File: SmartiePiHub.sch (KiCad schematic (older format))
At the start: 26 parts, among them P1 Conn_02x20_Odd_Even

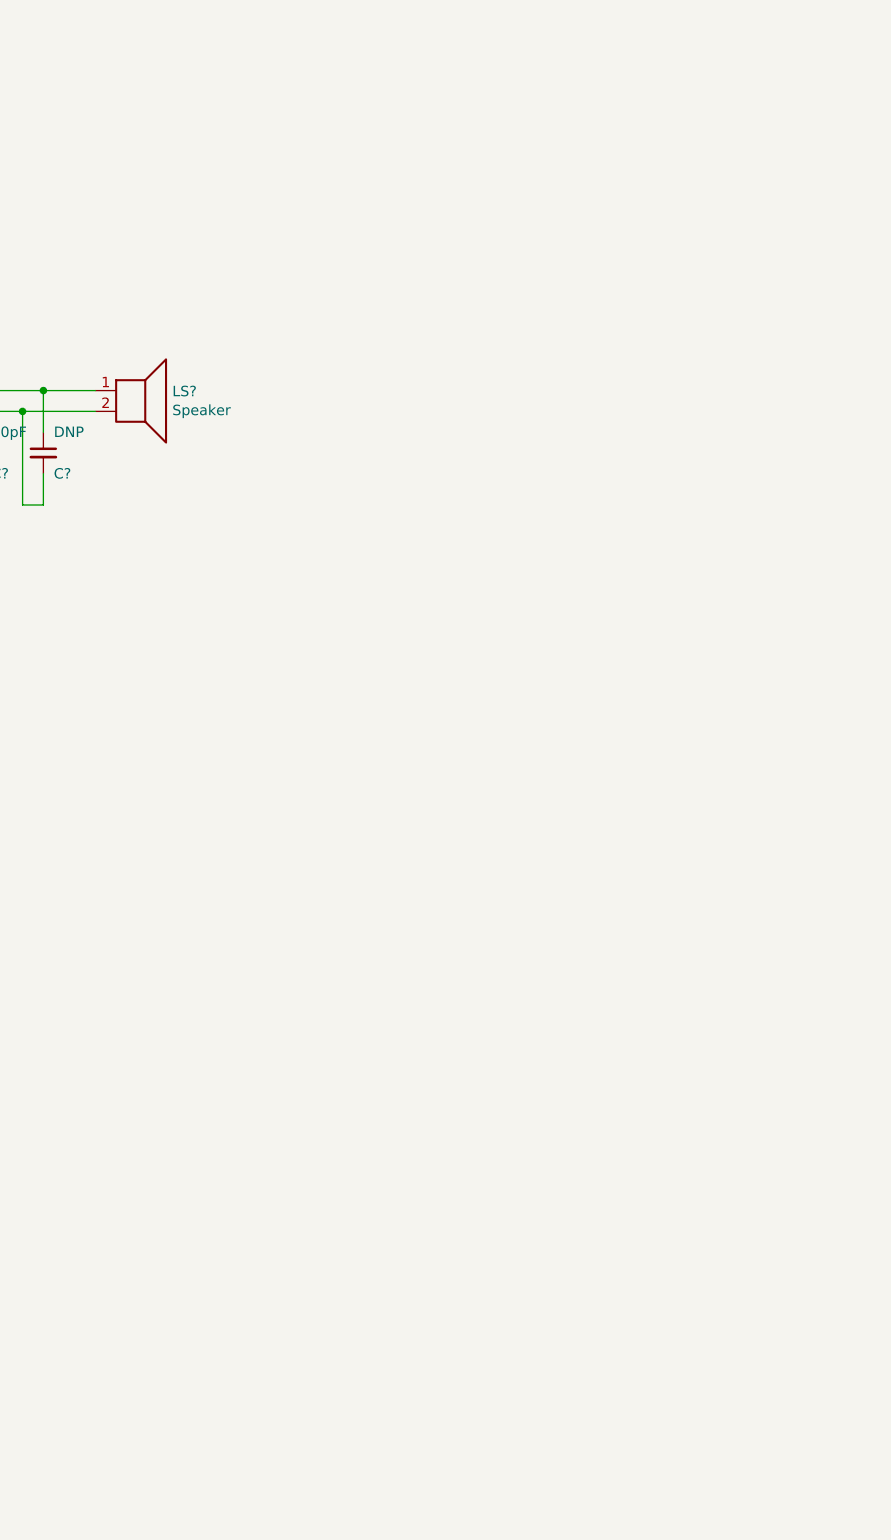
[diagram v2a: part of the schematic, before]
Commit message: added ina219 and mcp73833
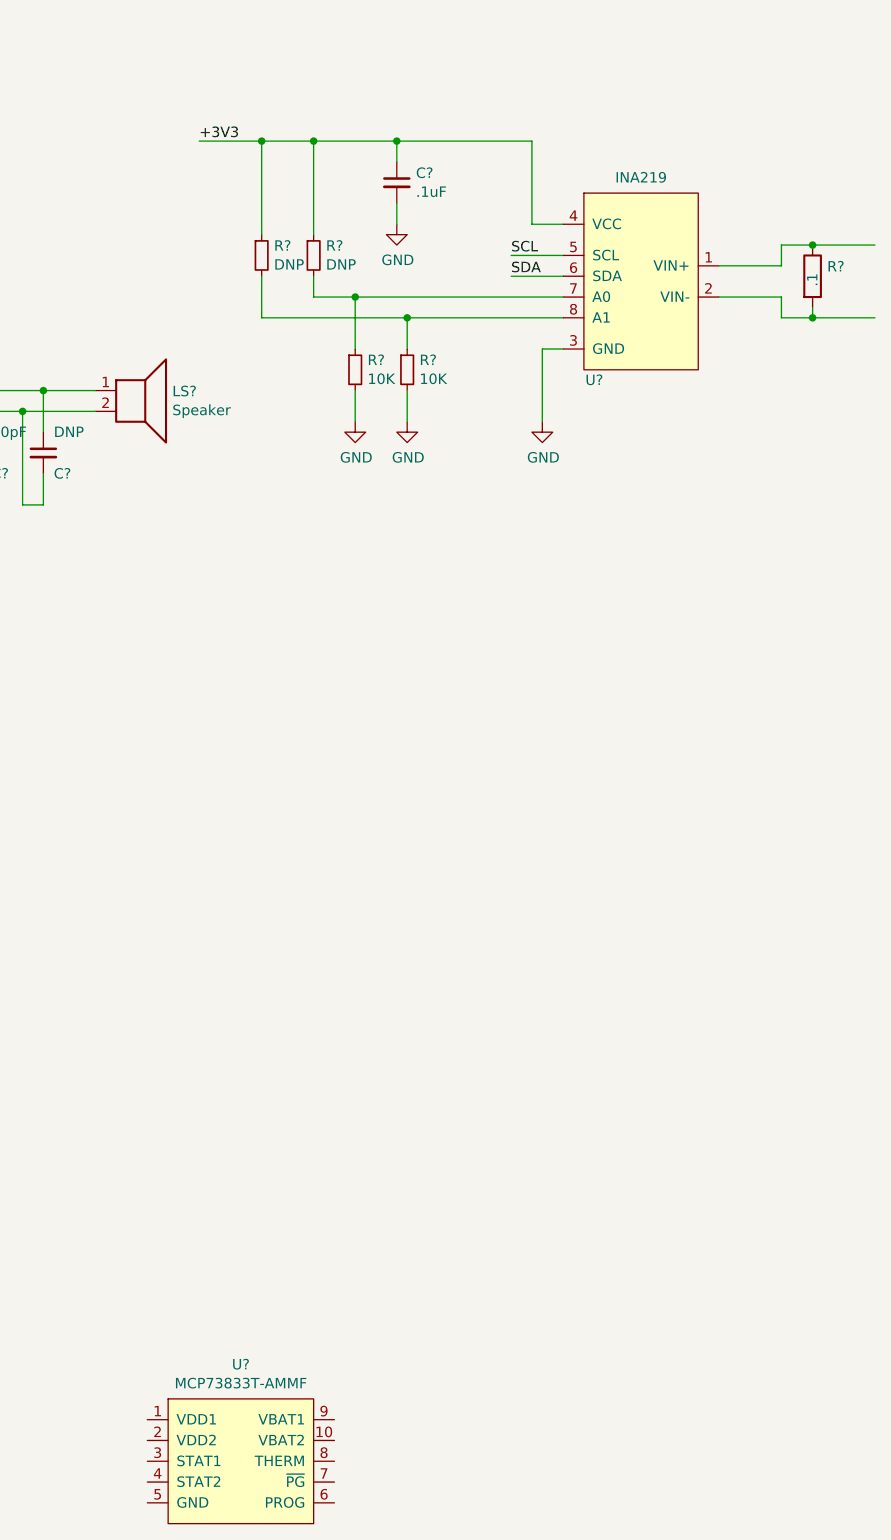
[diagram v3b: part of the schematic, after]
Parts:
- added C?: .1uF, symbol Device:C_Small
- added R? (x2): DNP, symbol Device:R_Small
- added R? (x2): 10K, symbol Device:R_Small
- added R?: .1, symbol Device:R
- added U?: INA219, symbol smartie-pi-hub:INA219
- added U?: MCP73833T-AMMF, symbol smartie-pi-hub:MCP73833T-AMMF
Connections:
- net +3V3: now also C?.1, R?.1, R?.1, U?.4 (VCC)
- net GND: now also C?.2, R?.2, R?.2, U?.3 (GND)
- new net: R?.1, U?.1 (VIN+)
- new net: R?.2, U?.2 (VIN-)
- new net: R?.1, R?.2, U?.7 (A0)
- new net: R?.1, R?.2, U?.8 (A1)
- new net SCL: U?.5 (SCL)
- new net SDA: U?.6 (SDA)
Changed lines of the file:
@@
 EELAYER 30 0
 EELAYER END
-$Descr A4 11693 8268
+$Descr A3 16535 11693
 encoding utf-8
 Sheet 1 1
@@
 	1    0    0    -1
 $EndComp
+$Comp
+L smartie-pi-hub:INA219 U?
+U 1 1 5EDB41F3
+P 13750 2050
+F 0 "U?" H 13500 1700 50  0000 C CNN
+F 1 "INA219" H 13725 2674 50  0000 C CNN
+F 2 "" H 13750 2050 50  0001 C CNN
+F 3 "" H 13750 2050 50  0001 C CNN
+	1    13750 2050
+	1    0    0    -1
+$EndComp
+$Comp
+L Device:C_Small C?
+U 1 1 5EDB4D7C
+P 12550 1450
+F 0 "C?" H 12642 1496 50  0000 L CNN
+F 1 ".1uF" H 12642 1405 50  0000 L CNN
+F 2 "" H 12550 1450 50  0001 C CNN
+F 3 "~" H 12550 1450 50  0001 C CNN
+	1    12550 1450
+	1    0    0    -1
+$EndComp
+$Comp
+L Device:R_Small R?
+U 1 1 5EDB5D3C
+P 12150 1800
+F 0 "R?" H 12209 1846 50  0000 L CNN
+F 1 "DNP" H 12209 1755 50  0000 L CNN
+F 2 "" H 12150 1800 50  0001 C CNN
+F 3 "~" H 12150 1800 50  0001 C CNN
+	1    12150 1800
+	1    0    0    -1
+$EndComp
+$Comp
+L Device:R_Small R?
+U 1 1 5EDB6AA8
+P 11900 1800
+F 0 "R?" H 11959 1846 50  0000 L CNN
+F 1 "DNP" H 11959 1755 50  0000 L CNN
+F 2 "" H 11900 1800 50  0001 C CNN
+F 3 "~" H 11900 1800 50  0001 C CNN
+	1    11900 1800
+	1    0    0    -1
+$EndComp
+$Comp
+L Device:R_Small R?
+U 1 1 5EDB758D
+P 12350 2350
+F 0 "R?" H 12409 2396 50  0000 L CNN
+F 1 "10K" H 12409 2305 50  0000 L CNN
+F 2 "" H 12350 2350 50  0001 C CNN
+F 3 "~" H 12350 2350 50  0001 C CNN
+	1    12350 2350
+	1    0    0    -1
+$EndComp
+$Comp
+L Device:R_Small R?
+U 1 1 5EDB7587
+P 12600 2350
+F 0 "R?" H 12659 2396 50  0000 L CNN
+F 1 "10K" H 12659 2305 50  0000 L CNN
+F 2 "" H 12600 2350 50  0001 C CNN
+F 3 "~" H 12600 2350 50  0001 C CNN
+	1    12600 2350
+	1    0    0    -1
+$EndComp
+Wire Wire Line
+	13350 2250 13250 2250
+$Comp
+L power:GND #PWR?
+U 1 1 5EDC7C5A
+P 13250 2600
+F 0 "#PWR?" H 13250 2350 50  0001 C CNN
+F 1 "GND" H 13255 2427 50  0000 C CNN
+F 2 "" H 13250 2600 50  0001 C CNN
+F 3 "" H 13250 2600 50  0001 C CNN
+	1    13250 2600
+	1    0    0    -1
+$EndComp
+Wire Wire Line
+	13250 2250 13250 2600
+$Comp
+L power:GND #PWR?
+U 1 1 5EDD0454
+P 12600 2600
+F 0 "#PWR?" H 12600 2350 50  0001 C CNN
+F 1 "GND" H 12605 2427 50  0000 C CNN
+F 2 "" H 12600 2600 50  0001 C CNN
+F 3 "" H 12600 2600 50  0001 C CNN
+	1    12600 2600
+	1    0    0    -1
+$EndComp
+$Comp
+L power:GND #PWR?
+U 1 1 5EDD09EB
+P 12350 2600
+F 0 "#PWR?" H 12350 2350 50  0001 C CNN
+F 1 "GND" H 12355 2427 50  0000 C CNN
+F 2 "" H 12350 2600 50  0001 C CNN
+F 3 "" H 12350 2600 50  0001 C CNN
+	1    12350 2600
+	1    0    0    -1
+$EndComp
+Wire Wire Line
+	12350 2600 12350 2450
+Wire Wire Line
+	12600 2450 12600 2600
+Wire Wire Line
+	13350 2100 12600 2100
+Wire Wire Line
+	11900 2100 11900 1900
+Wire Wire Line
+	12150 1900 12150 2000
+Wire Wire Line
+	12150 2000 12350 2000
+Wire Wire Line
+	12600 2250 12600 2100
+Connection ~ 12600 2100
+Wire Wire Line
+	12600 2100 11900 2100
+Wire Wire Line
+	12350 2000 12350 2250
+Connection ~ 12350 2000
+Wire Wire Line
+	12350 2000 13350 2000
+Wire Wire Line
+	12550 1550 12550 1650
+$Comp
+L power:GND #PWR?
+U 1 1 5EE0BE4E
+P 12550 1650
+F 0 "#PWR?" H 12550 1400 50  0001 C CNN
+F 1 "GND" H 12555 1477 50  0000 C CNN
+F 2 "" H 12550 1650 50  0001 C CNN
+F 3 "" H 12550 1650 50  0001 C CNN
+	1    12550 1650
+	1    0    0    -1
+$EndComp
+Wire Wire Line
+	12150 1700 12150 1250
+Wire Wire Line
+	12150 1250 11900 1250
+Wire Wire Line
+	11900 1250 11900 1700
+Connection ~ 11900 1250
+Wire Wire Line
+	11900 1250 11600 1250
+Wire Wire Line
+	12550 1350 12550 1250
+Wire Wire Line
+	12550 1250 12150 1250
+Connection ~ 12150 1250
+Wire Wire Line
+	13350 1650 13200 1650
+Wire Wire Line
+	13200 1650 13200 1250
+Wire Wire Line
+	13200 1250 12550 1250
+Connection ~ 12550 1250
+Text Label 11600 1250 0    50   ~ 0
++3V3
+Wire Wire Line
+	13350 1800 13100 1800
+Wire Wire Line
+	13350 1900 13100 1900
+Text Label 13100 1800 0    50   ~ 0
+SCL
+Text Label 13100 1900 0    50   ~ 0
+SDA
+$Comp
+L Device:R R?
+U 1 1 5EE4572A
+P 14550 1900
+F 0 "R?" H 14620 1946 50  0000 L CNN
+F 1 ".1" V 14550 1850 50  0000 L CNN
+F 2 "" V 14480 1900 50  0001 C CNN
+F 3 "~" H 14550 1900 50  0001 C CNN
+	1    14550 1900
+	1    0    0    -1
+$EndComp
+Wire Wire Line
+	14550 1750 14400 1750
+Wire Wire Line
+	14400 1750 14400 1850
+Wire Wire Line
+	14400 1850 14100 1850
+Wire Wire Line
+	14100 2000 14400 2000
+Wire Wire Line
+	14400 2000 14400 2100
+Wire Wire Line
+	14400 2100 14550 2100
+Wire Wire Line
+	14550 2100 14550 2050
+Wire Wire Line
+	14550 1750 14850 1750
+Connection ~ 14550 1750
+Wire Wire Line
+	14550 2100 14850 2100
+Connection ~ 14550 2100
+$Comp
+L smartie-pi-hub:MCP73833T-AMMF U?
+U 1 1 5EE89BA3
+P 11900 7700
+F 0 "U?" H 11800 8265 50  0000 C CNN
+F 1 "MCP73833T-AMMF" H 11800 8174 50  0000 C CNN
+F 2 "" H 11900 7700 50  0001 C CNN
+F 3 "" H 11900 7700 50  0001 C CNN
+	1    11900 7700
+	1    0    0    -1
+$EndComp

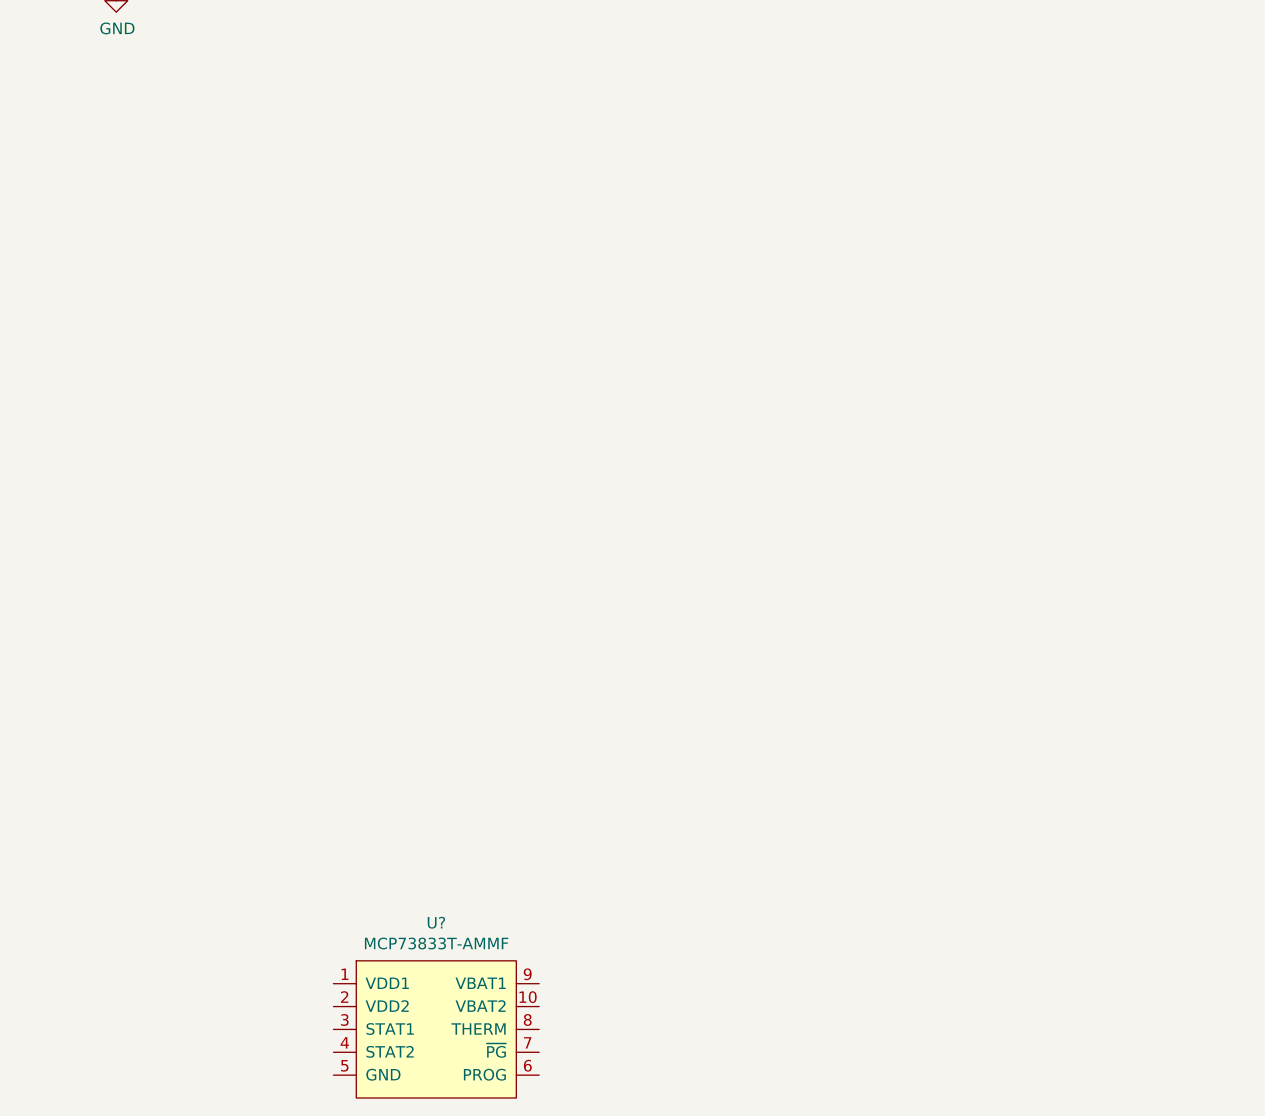
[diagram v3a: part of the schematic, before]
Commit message: added xc6206 circuit
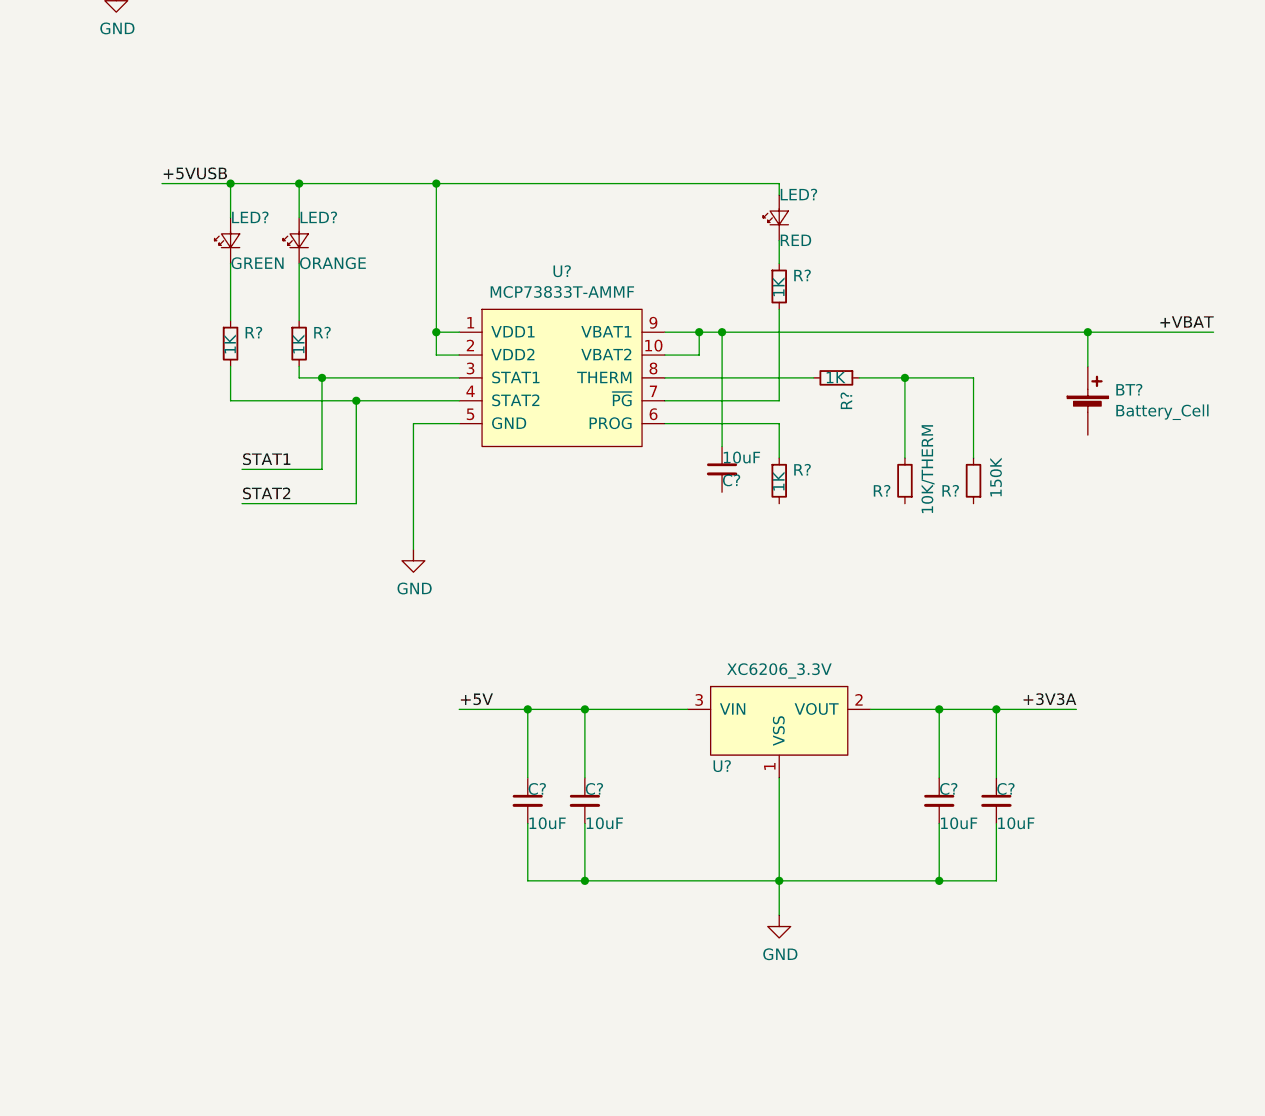
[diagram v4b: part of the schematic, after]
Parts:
- added BT?: Battery_Cell, symbol Device:Battery_Cell
- added C? (x5): 10uF, symbol Device:C_Small
- added LED?: ORANGE, symbol Device:LED_Small
- added LED?: GREEN, symbol Device:LED_Small
- added LED?: RED, symbol Device:LED_Small
- added R? (x5): 1K, symbol Device:R_Small
- added R?: 10K/THERM, symbol Device:R_Small
- added R?: 150K, symbol Device:R_Small
- added U?: XC6206_3.3V, symbol smartie-pi-hub:XC6206
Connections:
- net +3V3A: now also C?.1, C?.1, U?.2 (VOUT)
- net +5V: now also C?.1, C?.1, U?.3 (VIN)
- net GND: now also U?.5 (GND), C?.2, C?.2, C?.2, C?.2, U?.1 (VSS)
- net +5VUSB: now reaches U?.1 (VDD1)
- net +5VUSB: now also U?.2 (VDD2), LED?.2 (A), LED?.2 (A), LED?.2 (A)
- net +VBAT: now reaches U?.10 (VBAT2)
- net +VBAT: now also U?.9 (VBAT1), BT?.1 (+), C?.1
- net STAT1: now reaches U?.3 (STAT1)
- net STAT1: now also R?.2
- net STAT2: now reaches U?.4 (STAT2)
- net STAT2: now also R?.2
- net at U?.6 (PROG): now also R?.1
- net at U?.7 (~PG): now also R?.2
- net at U?.8 (THERM): now also R?.2
- new net: LED?.1 (K), R?.1 (x3)
- new net: R?.1, R?.2, R?.2
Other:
- moved on the sheet: U?

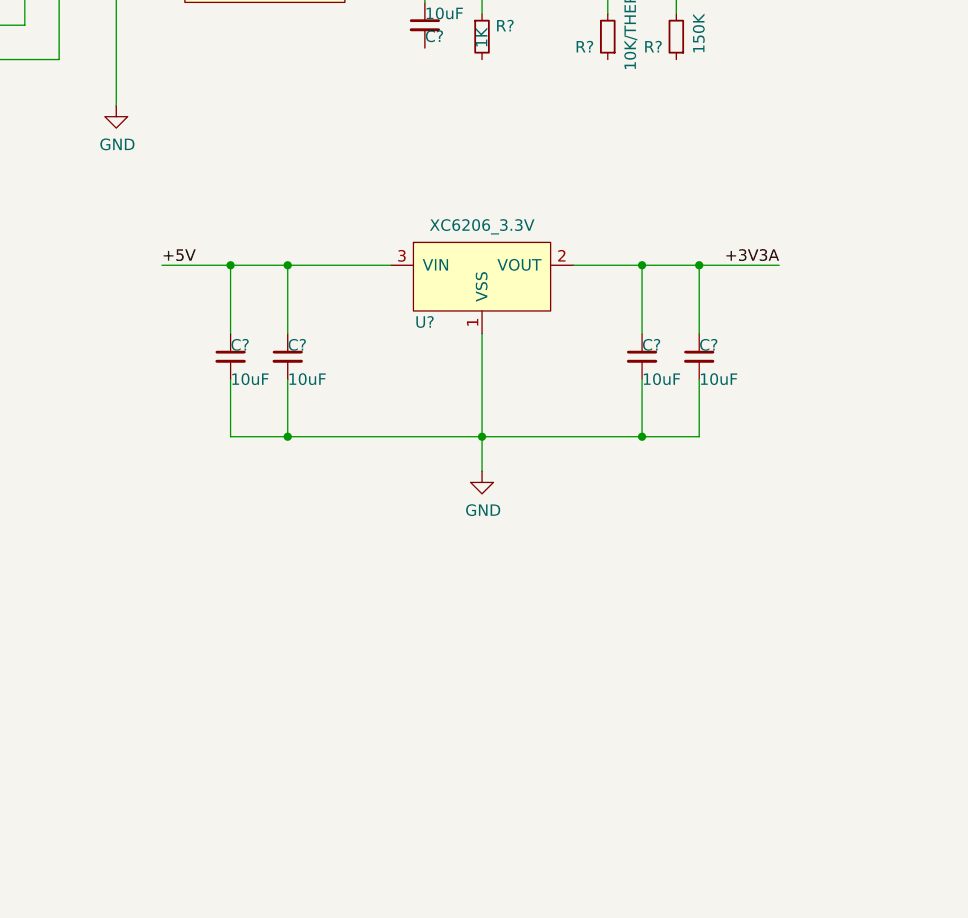
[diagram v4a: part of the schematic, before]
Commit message: added tps613222a circuit
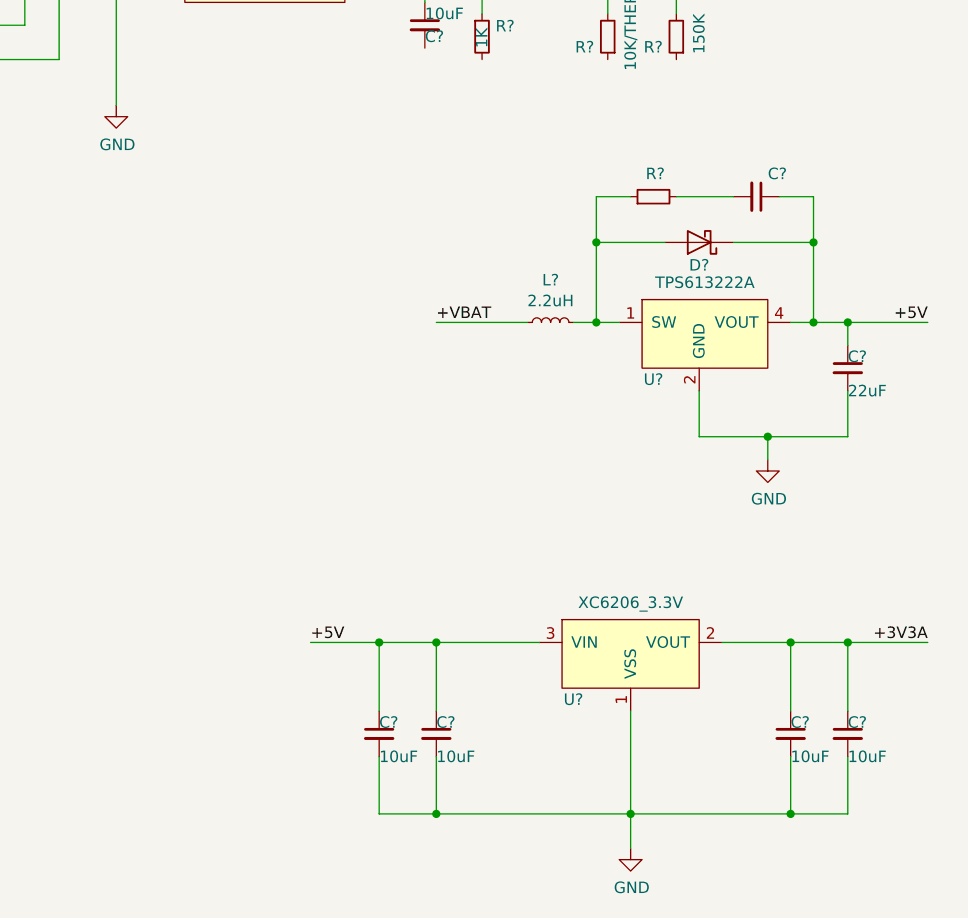
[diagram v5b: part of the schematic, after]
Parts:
- added C?: 22uF, symbol Device:C_Small
- added C?: snub cap, symbol Device:C_Small
- added D?: D_Schottky, symbol Device:D_Schottky
- added L?: 2.2uH, symbol Device:L_Small
- added R?: snub res, symbol Device:R_Small
- added U?: TPS613222A, symbol smartie-pi-hub:TPS613222A
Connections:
- net +5V: now also C?.1, C?.1, D?.1 (K), U?.4 (VOUT)
- net +VBAT: now also L?.1
- net GND: now also C?.2, U?.2 (GND)
- new net: D?.2 (A), L?.2, R?.1, U?.1 (SW)
- new net: C?.2, R?.2
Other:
- moved on the sheet: C?, U?
